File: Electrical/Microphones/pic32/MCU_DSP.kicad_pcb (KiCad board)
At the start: 2 copper layers, 51.5 x 36 mm, 28 parts, among them IC1 PIC32MK0128MCA048-I_Y8X, J1 Conn_01x05_Pin, J2 Conn_01x06, J3 Conn_01x06, J4 Conn_01x05, J5 Conn_01x06, J6 Conn_01x05, J7 UART, SW1 B3F-1020, SW2 SW_SPDT, U1 GSF7002DW

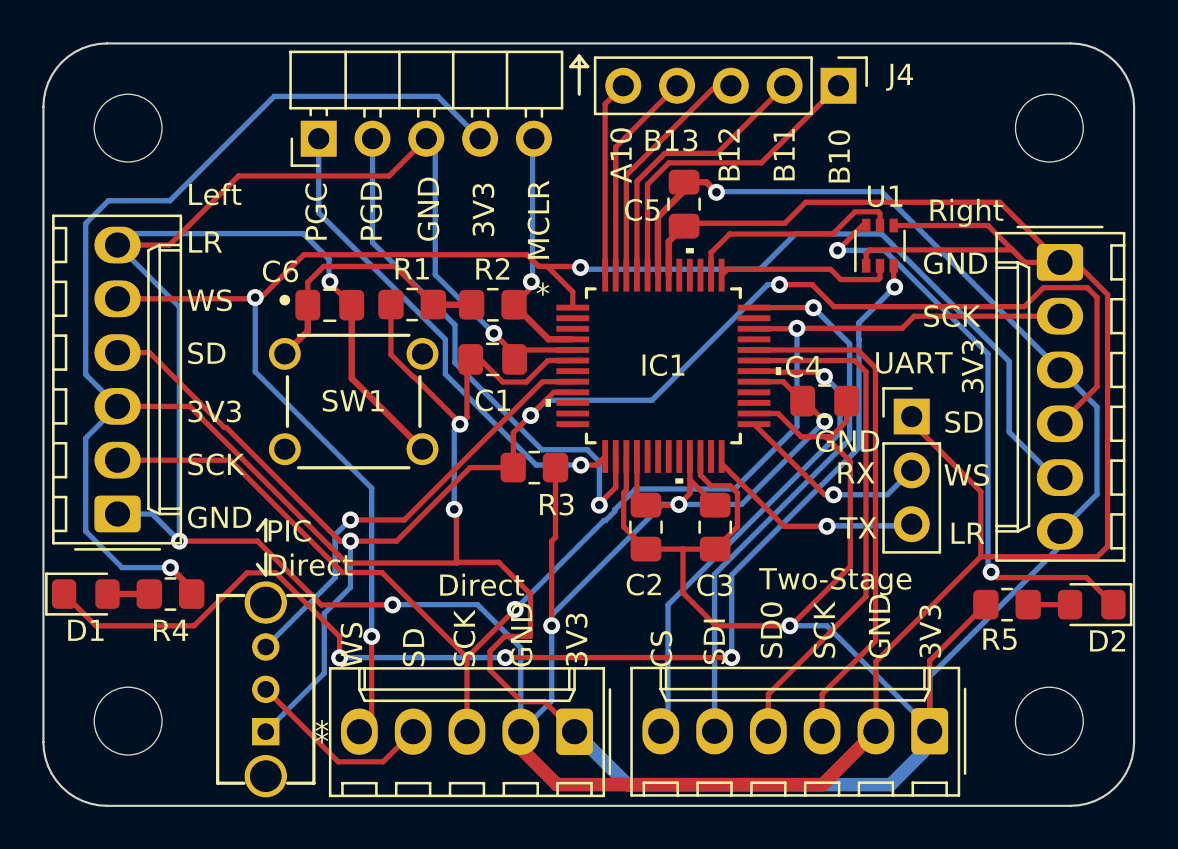
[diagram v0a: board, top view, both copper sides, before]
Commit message: Add updated Mic MCU board
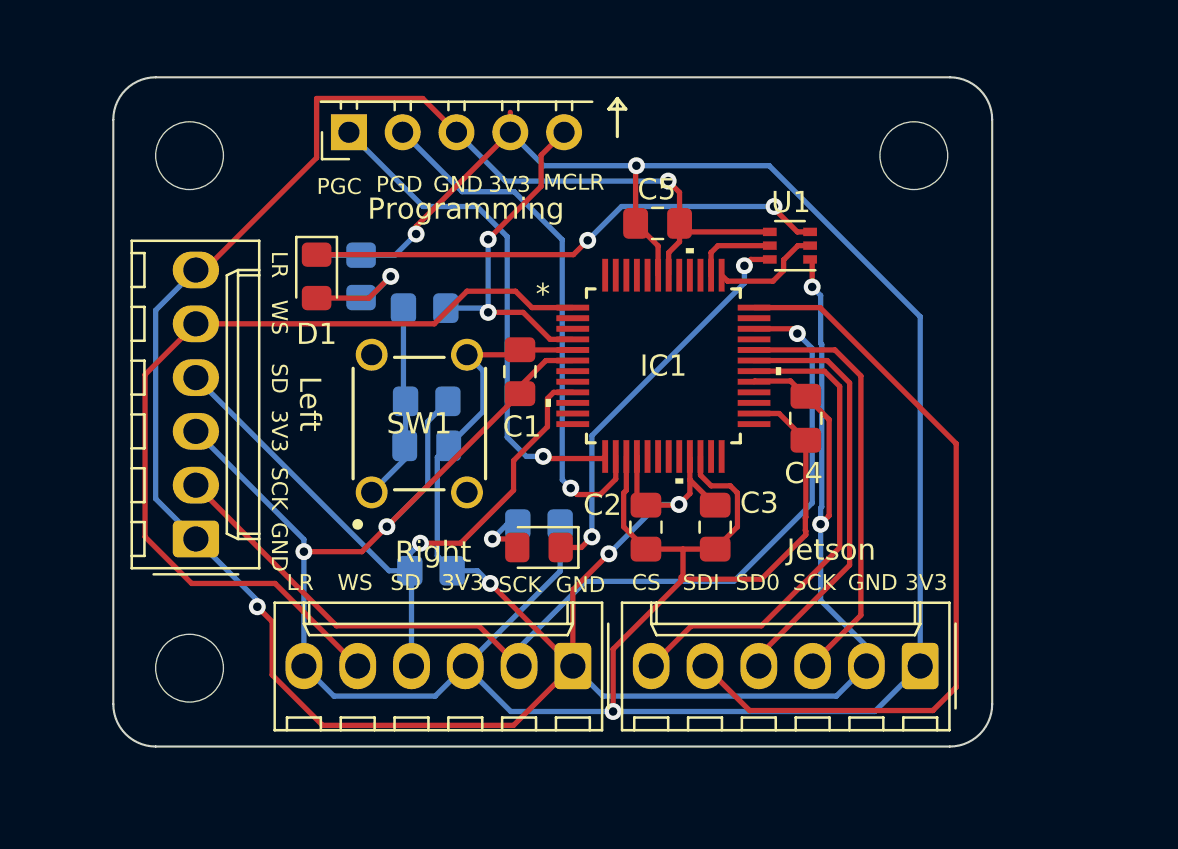
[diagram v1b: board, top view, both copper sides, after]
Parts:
- removed H4: MountingHole, MountingHole:MountingHole_3.2mm_M3
- removed J4: Conn_01x05, Connector_PinHeader_2.54mm:PinHeader_1x05_P2.54mm_Vertical
- removed J6: Conn_01x05, Connector_Molex:Molex_KK-254_AE-6410-05A_1x05_P2.54mm_Vertical
- removed J7: UART, Connector_PinHeader_2.54mm:PinHeader_1x03_P2.54mm_Vertical
- removed SW2: SW_SPDT, custom_footprints:SPDT_OS102011_CNK
- C6, R1, R2, R3, R4, R5: moved to B.Cu
- moved H3 40.7 mm to (188.9, 159.5)
- moved J3 29.9 mm to (207.0, 159.4), turned to 180 degrees
- moved D2 26.2 mm to (205.4, 153.8)
- moved R5 22.4 mm to (205.4, 152.7), turned to 180 degrees
- moved D1 18.5 mm to (194.9, 141.0), turned to -90 degrees
- moved R4 17.5 mm to (197.0, 141.0), turned to -90 degrees
- moved C6 8.07 mm to (200.1, 149.0)
- moved SW1 7.72 mm to (197.5, 151.2), turned to 90 degrees
- moved R3 6.89 mm to (200.3, 154.9)
- moved H2 6.53 mm to (223.1, 135.3)
- moved R1 4.62 mm to (200.1, 146.9), turned to 180 degrees
- moved U1 4.25 mm to (217.2, 139.6), turned to 180 degrees
- moved J2 3.88 mm to (189.2, 153.4)
- moved R2 3.22 mm to (200.0, 142.5)
- moved H1 3.18 mm to (188.9, 135.3)
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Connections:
- IC1 pad 24: Net-(IC1-TDI_/_FLT15_/_RPB4_/_SCL2_/_RB4) -> unconnected-(IC1-TDI_/_FLT15_/_RPB4_/_SCL2_/_RB4-Pad24)
- IC1 pad 25: Net-(IC1-AN13_/_RPA4_/_T1G_/_RA4) -> unconnected-(IC1-AN13_/_RPA4_/_T1G_/_RA4-Pad25)
- IC1 pad 44: Net-(IC1-TDO_/_RPB10_/_PWMH3_/_RB10) -> unconnected-(IC1-TDO_/_RPB10_/_PWMH3_/_RB10-Pad44)
- IC1 pad 45: Net-(IC1-TCK_/_RPB11_/_PWML3_/_RB11) -> unconnected-(IC1-TCK_/_RPB11_/_PWML3_/_RB11-Pad45)
- IC1 pad 46: Net-(IC1-RPB12_/_PWMH2_/_RB12) -> unconnected-(IC1-RPB12_/_PWMH2_/_RB12-Pad46)
- IC1 pad 47: Net-(IC1-RPB13_/_PWML2_/_CTPLS_/_RB13) -> unconnected-(IC1-RPB13_/_PWML2_/_CTPLS_/_RB13-Pad47)
- IC1 pad 48: Net-(IC1-PWMH4_/_RA10) -> unconnected-(IC1-PWMH4_/_RA10-Pad48)
- IC1 pad 8: Net-(IC1-AN10_/_C2IN4-_/_RPA11_/_FLT14_/_RA11) -> unconnected-(IC1-AN10_/_C2IN4-_/_RPA11_/_FLT14_/_RA11-Pad8)
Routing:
- net GND: track 229.6 -> 161.8 mm
- net +3V3: track 219.1 -> 172.2 mm
- net Net-(IC1-OA2OUT_/_AN0_/_C2IN2-_/_RPA0_/_RA0): track 76.7 -> 31.5 mm, vias 3 -> 1
- net Net-(IC1-RPA7_/_PWML4_/_RA7): track 77.9 -> 42.4 mm, vias 3 -> 0
- net Net-(D1-K): track 57.2 -> 24.8 mm, vias 4 -> 2
- net Net-(IC1-AN10_/_C2IN4-_/_RPA11_/_FLT14_/_RA11): track 20.9 -> 0.00 mm, vias 1 -> 0
- net Net-(IC1-AN15_/_RPB7_/_SCK1_/_INT0_/_RB7): track 63.3 -> 45.9 mm, vias 2 -> 1
- net Net-(IC1-TDO_/_RPB10_/_PWMH3_/_RB10): track 15.2 -> 0.00 mm
- net Net-(IC1-TCK_/_RPB11_/_PWML3_/_RB11): track 13.3 -> 0.00 mm
- net Net-(IC1-SOSCO_/_RPB8_/_T1CK_/_RB8): track 26.2 -> 36.9 mm, vias 1 -> 0
- net Net-(IC1-RPB12_/_PWMH2_/_RB12): track 10.7 -> 0.00 mm
- net Net-(IC1-RPB13_/_PWML2_/_CTPLS_/_RB13): track 10.1 -> 0.00 mm
- net Net-(IC1-TDI_/_FLT15_/_RPB4_/_SCL2_/_RB4): track 10.1 -> 0.00 mm, vias 1 -> 0
- net Net-(IC1-PWMH4_/_RA10): track 9.30 -> 0.00 mm
- net Net-(IC1-AN13_/_RPA4_/_T1G_/_RA4): track 9.02 -> 0.00 mm, vias 1 -> 0
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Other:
- board size 51.5 x 36 mm -> 41.5 x 31.6 mm
- board text added: "34.2 mm x 24.2 mm hole spacing 41.5 mm x 31.6 mm board size"
- board text added: "Audio Processing Board PIC32MK0128MCA048-I_Y8X Ver. 2.0 --- 5/28/2025 Matthew Sato Engineering Informatics Group"
- board text added: "Jetson"
- board text added: "Programming"
- board text removed: "43.5 mm x 28.0 mm hole spacing 51.5 mm x 36 mm board size"
- board text removed: "A10"
- board text removed: "Audio Processing Board PIC32MK0128MCA048-I_Y8X Ver. 1.0 --- 9/26/2024 Matthew Sato Engineering Informatics Group"
- board text removed: "B10"
- board text removed: "B11"
- board text removed: "B12"
- board text removed: "B13"
- board text removed: "Direct"
- board text removed: "PIC Direct"
- board text removed: "RX"
- board text removed: "TX"
- board text removed: "Two-Stage"
- board text removed: "UART"
